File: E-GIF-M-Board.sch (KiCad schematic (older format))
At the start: 0 parts

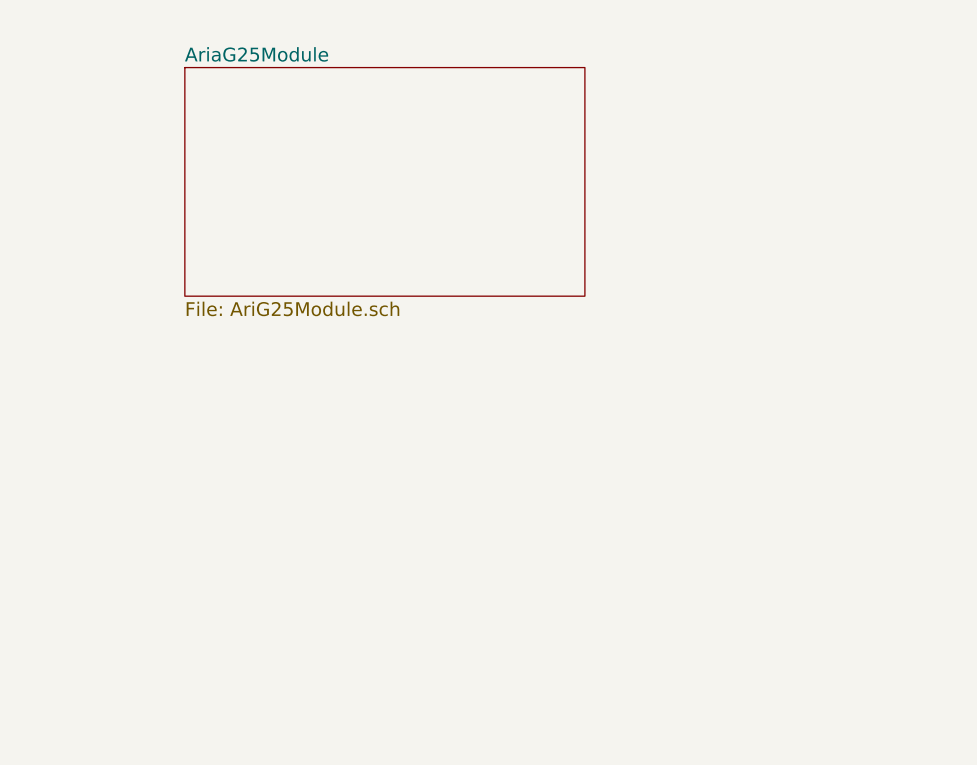
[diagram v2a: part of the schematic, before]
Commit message: Moved and connected the Debug, MicroSD and EthernetIN(EthIN) in the Interfaces schematic.
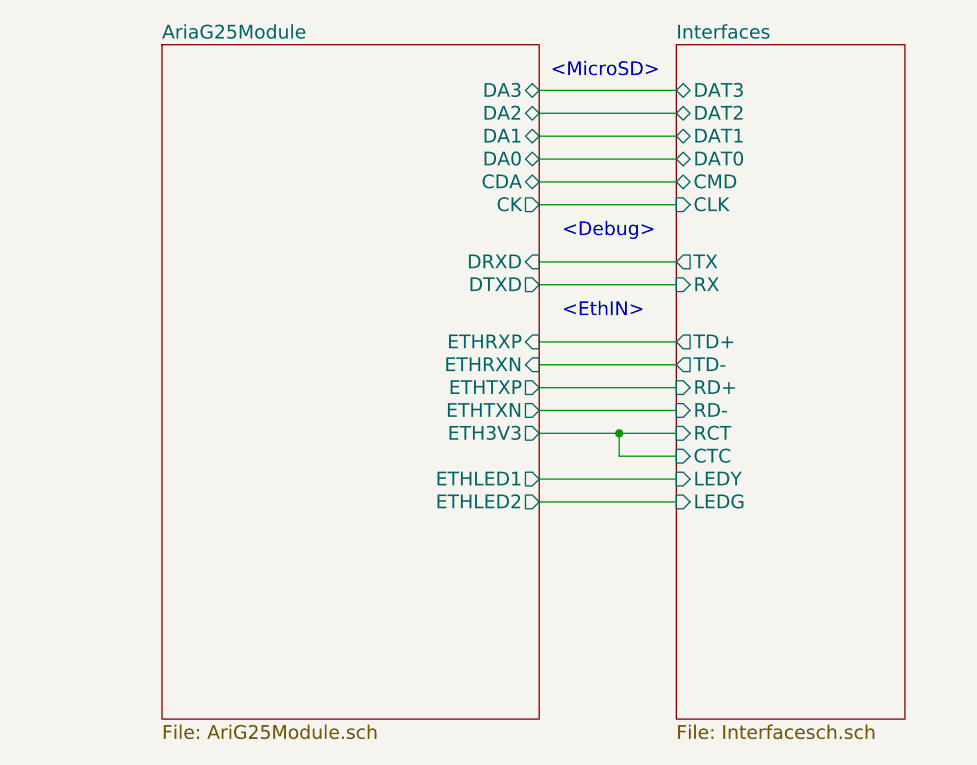
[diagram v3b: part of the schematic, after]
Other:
- note added: "<Debug>"
- note added: "<EthIN>"
- note added: "<MicroSD>"
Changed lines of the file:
@@
 $Descr A4 11693 8268
 encoding utf-8
-Sheet 1 3
+Sheet 1 4
 Title "E-GIF-M Board"
 Date "2017-01-15"
@@
 $EndSheet
 $Sheet
-S 5750 2200 1750 1000
+S 5650 2100 1650 2950
 U 587D31F1
 F0 "AriaG25Module" 60
 F1 "AriG25Module.sch" 60
+F2 "DA0" B R 7300 2600 60
+F3 "CDA" B R 7300 2700 60
+F4 "CK" O R 7300 2800 60
+F5 "DA1" B R 7300 2500 60
+F6 "DA2" B R 7300 2400 60
+F7 "DA3" B R 7300 2300 60
+F8 "DRXD" I R 7300 3050 60
+F9 "DTXD" O R 7300 3150 60
+F10 "ETHRXP" I R 7300 3400 60
+F11 "ETHRXN" I R 7300 3500 60
+F12 "ETHTXP" O R 7300 3600 60
+F13 "ETHTXN" O R 7300 3700 60
+F14 "ETH3V3" O R 7300 3800 60
+F15 "ETHLED1" O R 7300 4000 60
+F16 "ETHLED2" O R 7300 4100 60
 $EndSheet
+$Sheet
+S 7900 2100 1000 2950
+U 587FE94B
+F0 "Interfaces" 60
+F1 "Interfacesch.sch" 60
+F2 "DAT2" B L 7900 2400 60
+F3 "DAT3" B L 7900 2300 60
+F4 "CMD" B L 7900 2700 60
+F5 "CLK" I L 7900 2800 60
+F6 "DAT0" B L 7900 2600 60
+F7 "DAT1" B L 7900 2500 60
+F8 "RX" I L 7900 3150 60
+F9 "TX" O L 7900 3050 60
+F10 "RD+" I L 7900 3600 60
+F11 "RCT" I L 7900 3800 60
+F12 "RD-" I L 7900 3700 60
+F13 "TD+" O L 7900 3400 60
+F14 "CTC" I L 7900 3900 60
+F15 "TD-" O L 7900 3500 60
+F16 "LEDG" I L 7900 4100 60
+F17 "LEDY" I L 7900 4000 60
+$EndSheet
+Text Notes 7350 2250 0    60   ~ 0
+<MicroSD>
+Wire Wire Line
+	7300 2300 7900 2300
+Wire Wire Line
+	7300 2400 7900 2400
+Wire Wire Line
+	7300 2500 7900 2500
+Wire Wire Line
+	7300 2600 7900 2600
+Wire Wire Line
+	7300 2700 7900 2700
+Wire Wire Line
+	7300 2800 7900 2800
+Text Notes 7400 2950 0    60   ~ 0
+<Debug>
+Text Notes 7400 3300 0    60   ~ 0
+<EthIN>
+Wire Wire Line
+	7300 3150 7900 3150
+Wire Wire Line
+	7300 3050 7900 3050
+Wire Wire Line
+	7300 4000 7900 4000
+Wire Wire Line
+	7300 4100 7900 4100
+Wire Wire Line
+	7300 3800 7900 3800
+Wire Wire Line
+	7900 3900 7650 3900
+Wire Wire Line
+	7650 3900 7650 3800
+Connection ~ 7650 3800
+Wire Wire Line
+	7300 3400 7900 3400
+Wire Wire Line
+	7300 3500 7900 3500
+Wire Wire Line
+	7300 3600 7900 3600
+Wire Wire Line
+	7300 3700 7900 3700
 $EndSCHEMATC

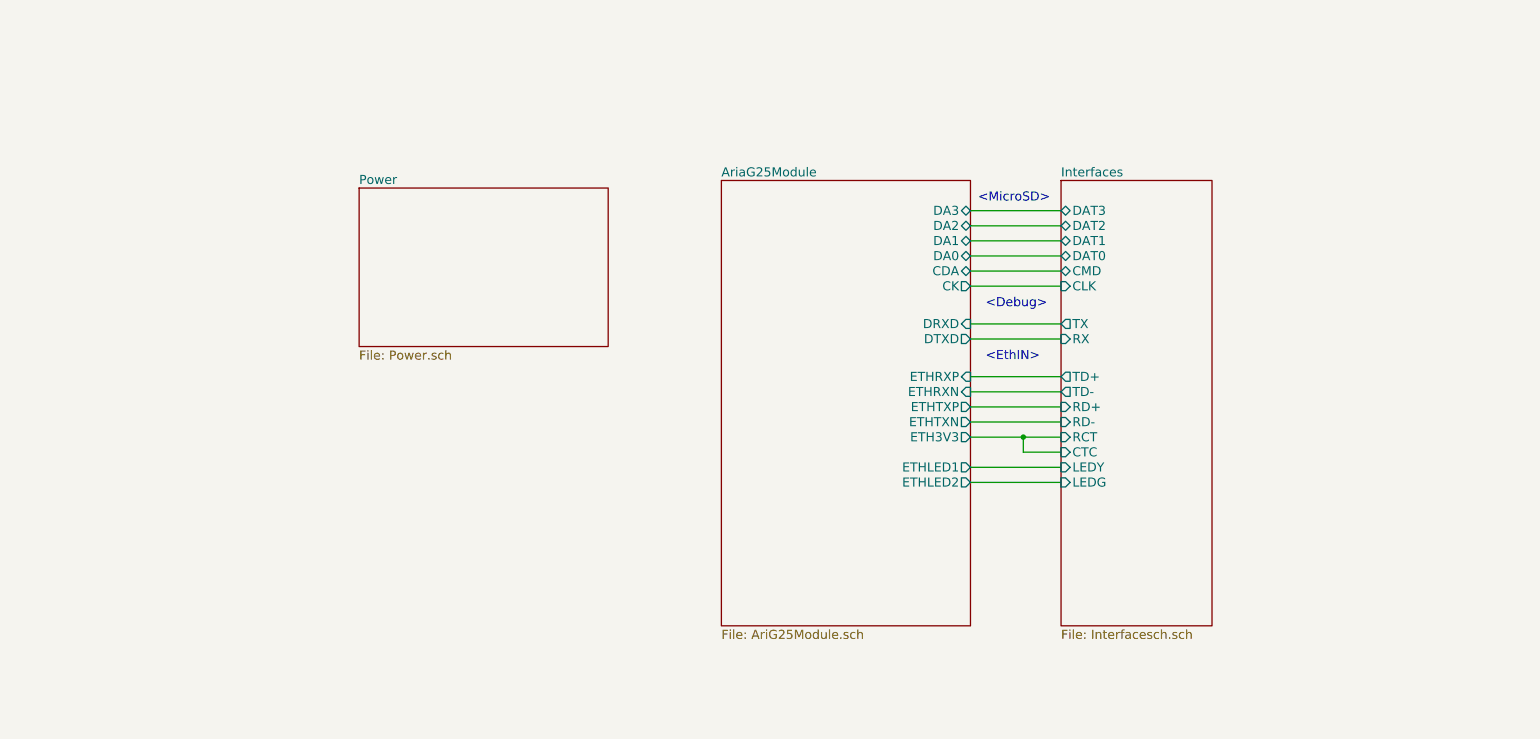
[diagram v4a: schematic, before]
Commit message: Finished LAN9500A ETH to USB interface sheet.
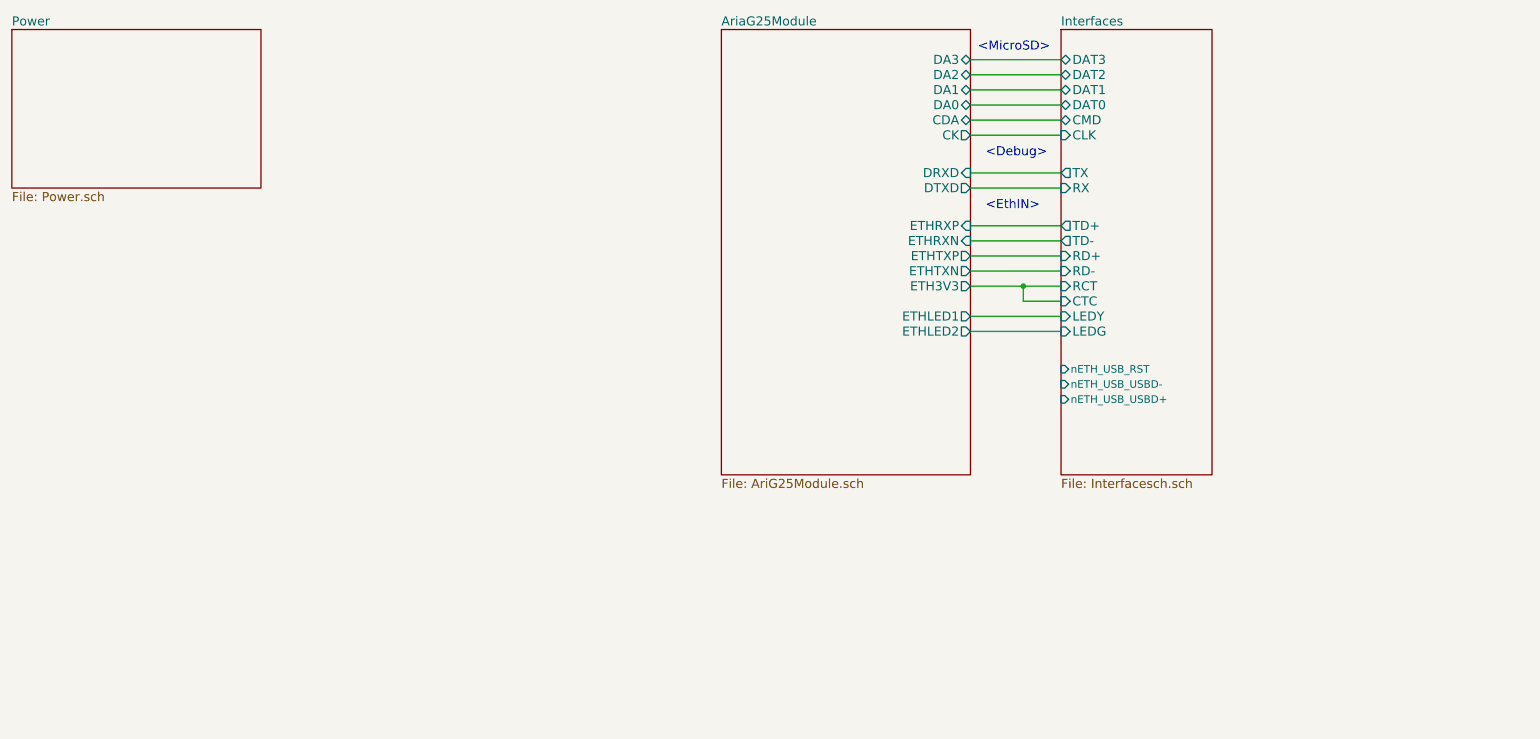
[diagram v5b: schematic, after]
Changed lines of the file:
@@
 $EndDescr
 $Sheet
-S 3250 2150 1650 1050
+S 950  1100 1650 1050
 U 587BDB63
 F0 "Power" 60
@@
 $EndSheet
 $Sheet
-S 5650 2100 1650 2950
+S 5650 1100 1650 2950
 U 587D31F1
 F0 "AriaG25Module" 60
 F1 "AriG25Module.sch" 60
-F2 "DA0" B R 7300 2600 60
-F3 "CDA" B R 7300 2700 60
-F4 "CK" O R 7300 2800 60
-F5 "DA1" B R 7300 2500 60
-F6 "DA2" B R 7300 2400 60
-F7 "DA3" B R 7300 2300 60
-F8 "DRXD" I R 7300 3050 60
-F9 "DTXD" O R 7300 3150 60
-F10 "ETHRXP" I R 7300 3400 60
-F11 "ETHRXN" I R 7300 3500 60
-F12 "ETHTXP" O R 7300 3600 60
-F13 "ETHTXN" O R 7300 3700 60
-F14 "ETH3V3" O R 7300 3800 60
-F15 "ETHLED1" O R 7300 4000 60
-F16 "ETHLED2" O R 7300 4100 60
+F2 "DA0" B R 7300 1600 60
+F3 "CDA" B R 7300 1700 60
+F4 "CK" O R 7300 1800 60
+F5 "DA1" B R 7300 1500 60
+F6 "DA2" B R 7300 1400 60
+F7 "DA3" B R 7300 1300 60
+F8 "DRXD" I R 7300 2050 60
+F9 "DTXD" O R 7300 2150 60
+F10 "ETHRXP" I R 7300 2400 60
+F11 "ETHRXN" I R 7300 2500 60
+F12 "ETHTXP" O R 7300 2600 60
+F13 "ETHTXN" O R 7300 2700 60
+F14 "ETH3V3" O R 7300 2800 60
+F15 "ETHLED1" O R 7300 3000 60
+F16 "ETHLED2" O R 7300 3100 60
 $EndSheet
 $Sheet
-S 7900 2100 1000 2950
+S 7900 1100 1000 2950
 U 587FE94B
 F0 "Interfaces" 60
 F1 "Interfacesch.sch" 60
-F2 "DAT2" B L 7900 2400 60
-F3 "DAT3" B L 7900 2300 60
-F4 "CMD" B L 7900 2700 60
-F5 "CLK" I L 7900 2800 60
-F6 "DAT0" B L 7900 2600 60
-F7 "DAT1" B L 7900 2500 60
-F8 "RX" I L 7900 3150 60
-F9 "TX" O L 7900 3050 60
-F10 "RD+" I L 7900 3600 60
-F11 "RCT" I L 7900 3800 60
-F12 "RD-" I L 7900 3700 60
-F13 "TD+" O L 7900 3400 60
-F14 "CTC" I L 7900 3900 60
-F15 "TD-" O L 7900 3500 60
-F16 "LEDG" I L 7900 4100 60
-F17 "LEDY" I L 7900 4000 60
+F2 "DAT2" B L 7900 1400 60
+F3 "DAT3" B L 7900 1300 60
+F4 "CMD" B L 7900 1700 60
+F5 "CLK" I L 7900 1800 60
+F6 "DAT0" B L 7900 1600 60
+F7 "DAT1" B L 7900 1500 60
+F8 "RX" I L 7900 2150 60
+F9 "TX" O L 7900 2050 60
+F10 "RD+" I L 7900 2600 60
+F11 "RCT" I L 7900 2800 60
+F12 "RD-" I L 7900 2700 60
+F13 "TD+" O L 7900 2400 60
+F14 "CTC" I L 7900 2900 60
+F15 "TD-" O L 7900 2500 60
+F16 "LEDG" I L 7900 3100 60
+F17 "LEDY" I L 7900 3000 60
+F18 "nETH_USB_RST" I L 7900 3350 50
+F19 "nETH_USB_USBD-" I L 7900 3450 50
+F20 "nETH_USB_USBD+" I L 7900 3550 50
 $EndSheet
-Text Notes 7350 2250 0    60   ~ 0
+Text Notes 7350 1250 0    60   ~ 0
 <MicroSD>
 Wire Wire Line
-	7300 2300 7900 2300
+	7300 1300 7900 1300
+Wire Wire Line
+	7300 1400 7900 1400
+Wire Wire Line
+	7300 1500 7900 1500
+Wire Wire Line
+	7300 1600 7900 1600
+Wire Wire Line
+	7300 1700 7900 1700
+Wire Wire Line
+	7300 1800 7900 1800
+Text Notes 7400 1950 0    60   ~ 0
+<Debug>
+Text Notes 7400 2300 0    60   ~ 0
+<EthIN>
+Wire Wire Line
+	7300 2150 7900 2150
+Wire Wire Line
+	7300 2050 7900 2050
+Wire Wire Line
+	7300 3000 7900 3000
+Wire Wire Line
+	7300 3100 7900 3100
+Wire Wire Line
+	7300 2800 7900 2800
+Wire Wire Line
+	7900 2900 7650 2900
+Wire Wire Line
+	7650 2900 7650 2800
+Connection ~ 7650 2800
 Wire Wire Line
 	7300 2400 7900 2400
@@
 Wire Wire Line
 	7300 2700 7900 2700
-Wire Wire Line
-	7300 2800 7900 2800
-Text Notes 7400 2950 0    60   ~ 0
-<Debug>
-Text Notes 7400 3300 0    60   ~ 0
-<EthIN>
-Wire Wire Line
-	7300 3150 7900 3150
-Wire Wire Line
-	7300 3050 7900 3050
-Wire Wire Line
-	7300 4000 7900 4000
-Wire Wire Line
-	7300 4100 7900 4100
-Wire Wire Line
-	7300 3800 7900 3800
-Wire Wire Line
-	7900 3900 7650 3900
-Wire Wire Line
-	7650 3900 7650 3800
-Connection ~ 7650 3800
-Wire Wire Line
-	7300 3400 7900 3400
-Wire Wire Line
-	7300 3500 7900 3500
-Wire Wire Line
-	7300 3600 7900 3600
-Wire Wire Line
-	7300 3700 7900 3700
 $EndSCHEMATC

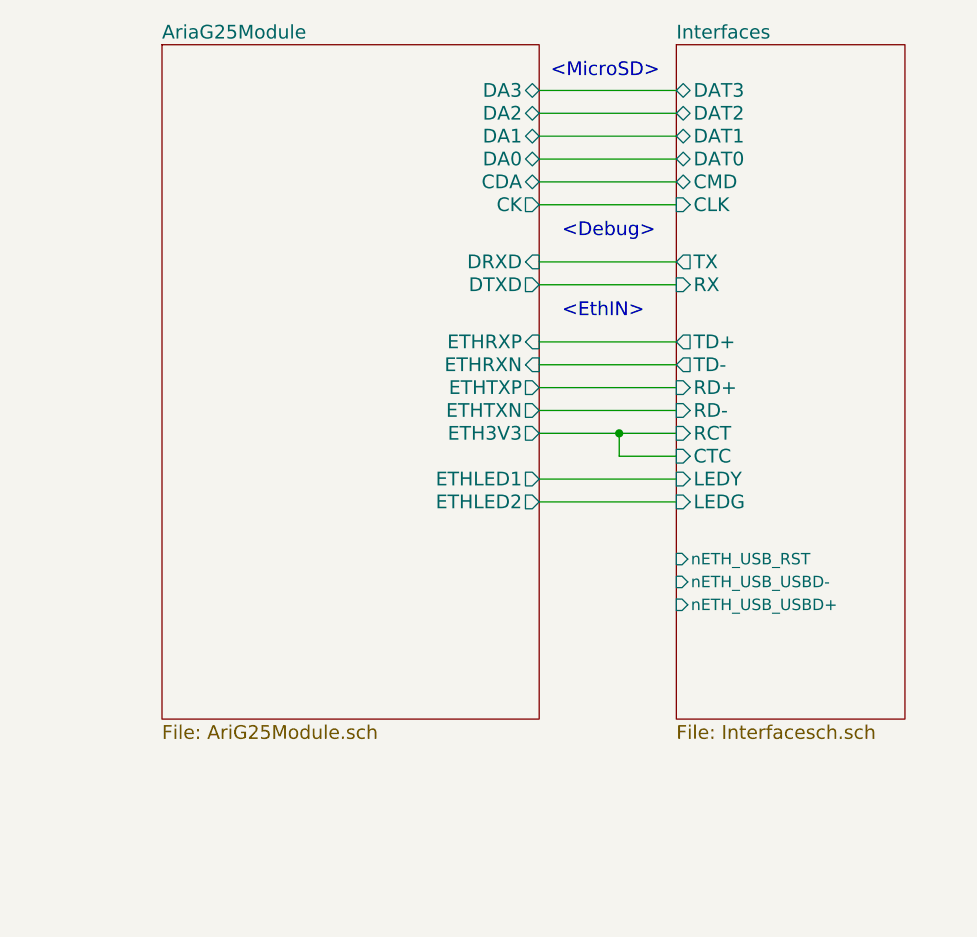
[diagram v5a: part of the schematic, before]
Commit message: Finished interfaces.
Finished MAX3232 serial to RS232 interface.
Finished ST3485 serial to RS485 interface.
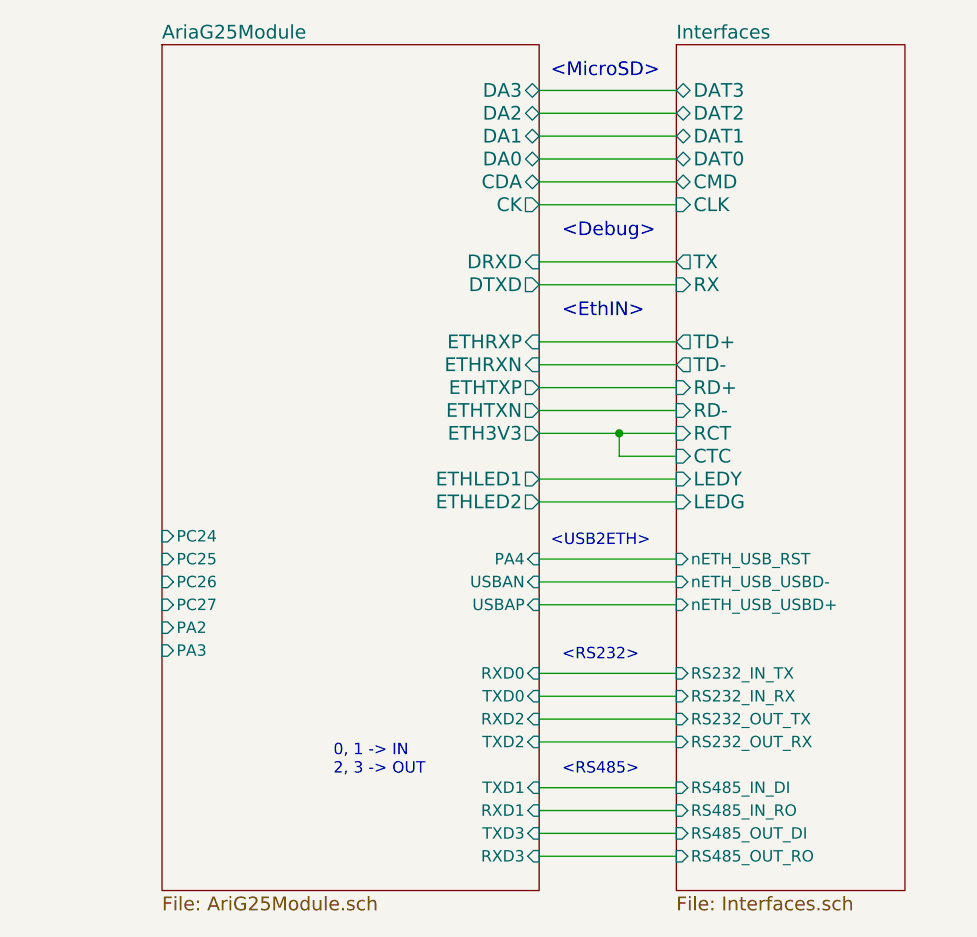
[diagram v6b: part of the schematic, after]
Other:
- note added: "0, 1 -> IN\n2, 3 -> OUT"
- note added: "<RS232>"
- note added: "<RS485>"
- note added: "<USB2ETH>"
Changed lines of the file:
@@
 LIBS:MCP2200
 LIBS:w_connectors
+LIBS:max-lin
 LIBS:E-GIF-M-Board-cache
 EELAYER 25 0
@@
 $Descr A4 11693 8268
 encoding utf-8
-Sheet 1 5
+Sheet 1 7
 Title "E-GIF-M Board"
 Date "2017-01-15"
@@
 $EndSheet
 $Sheet
-S 5650 1100 1650 2950
+S 5650 1100 1650 3700
 U 587D31F1
 F0 "AriaG25Module" 60
@@
 F15 "ETHLED1" O R 7300 3000 60
 F16 "ETHLED2" O R 7300 3100 60
+F17 "RXD2" I R 7300 4050 50
+F18 "TXD2" I R 7300 4150 50
+F19 "RXD1" I R 7300 4450 50
+F20 "TXD1" I R 7300 4350 50
+F21 "RXD0" I R 7300 3850 50
+F22 "TXD0" I R 7300 3950 50
+F23 "TXD3" I R 7300 4550 50
+F24 "RXD3" I R 7300 4650 50
+F25 "USBAP" I R 7300 3550 50
+F26 "USBAN" I R 7300 3450 50
+F27 "PC24" I L 5650 3250 50
+F28 "PC25" I L 5650 3350 50
+F29 "PC26" I L 5650 3450 50
+F30 "PC27" I L 5650 3550 50
+F31 "PA2" I L 5650 3650 50
+F32 "PA3" I L 5650 3750 50
+F33 "PA4" I R 7300 3350 50
 $EndSheet
 $Sheet
-S 7900 1100 1000 2950
+S 7900 1100 1000 3700
 U 587FE94B
 F0 "Interfaces" 60
-F1 "Interfacesch.sch" 60
+F1 "Interfaces.sch" 60
 F2 "DAT2" B L 7900 1400 60
 F3 "DAT3" B L 7900 1300 60
@@
 F19 "nETH_USB_USBD-" I L 7900 3450 50
 F20 "nETH_USB_USBD+" I L 7900 3550 50
+F21 "RS232_IN_TX" I L 7900 3850 50
+F22 "RS232_OUT_TX" I L 7900 4050 50
+F23 "RS232_OUT_RX" I L 7900 4150 50
+F24 "RS232_IN_RX" I L 7900 3950 50
+F25 "RS485_IN_DI" I L 7900 4350 50
+F26 "RS485_IN_RO" I L 7900 4450 50
+F27 "RS485_OUT_DI" I L 7900 4550 50
+F28 "RS485_OUT_RO" I L 7900 4650 50
 $EndSheet
 Text Notes 7350 1250 0    60   ~ 0
@@
 Wire Wire Line
 	7300 2700 7900 2700
+Wire Wire Line
+	7300 4350 7900 4350
+Wire Wire Line
+	7300 4450 7900 4450
+Wire Wire Line
+	7300 4550 7900 4550
+Wire Wire Line
+	7300 4650 7900 4650
+Text Notes 6400 4300 0    50   ~ 0
+0, 1 -> IN\n2, 3 -> OUT
+Wire Wire Line
+	7300 3850 7900 3850
+Wire Wire Line
+	7300 3950 7900 3950
+Wire Wire Line
+	7300 4050 7900 4050
+Wire Wire Line
+	7300 4150 7900 4150
+Wire Wire Line
+	7300 3350 7900 3350
+Wire Wire Line
+	7300 3450 7900 3450
+Wire Wire Line
+	7300 3550 7900 3550
+Text Notes 7350 3300 0    50   ~ 0
+<USB2ETH>
+Text Notes 7400 3800 0    50   ~ 0
+<RS232>
+Text Notes 7400 4300 0    50   ~ 0
+<RS485>
 $EndSCHEMATC

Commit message: Added some info text.
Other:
- note added: "<- Pentru RS232, RX la TX"
- note added: "<- Pentru RS485 DI la TX si RO laRX"
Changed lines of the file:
@@
 Text Notes 7400 4300 0    50   ~ 0
 <RS485>
+Text Notes 8900 4000 0    60   ~ 0
+<- Pentru RS232, RX la TX
+Text Notes 8900 4550 0    60   ~ 0
+<- Pentru RS485 DI la TX si RO laRX
 $EndSCHEMATC
